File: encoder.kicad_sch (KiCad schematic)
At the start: 0 parts

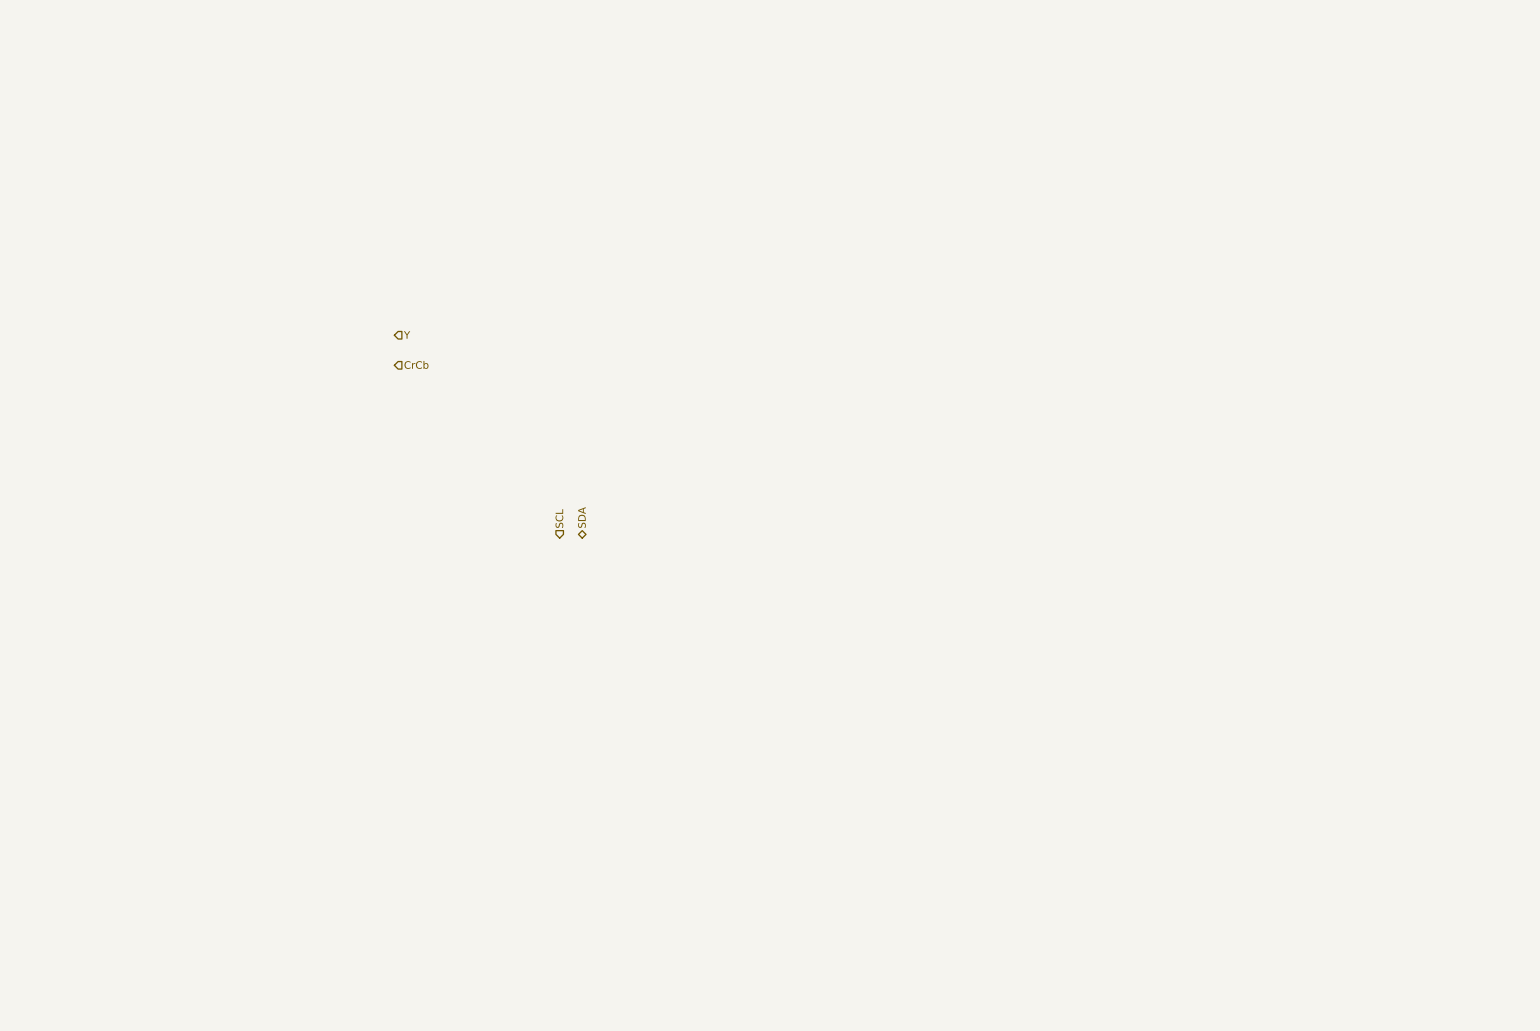
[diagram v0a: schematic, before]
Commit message: added decoder symbol
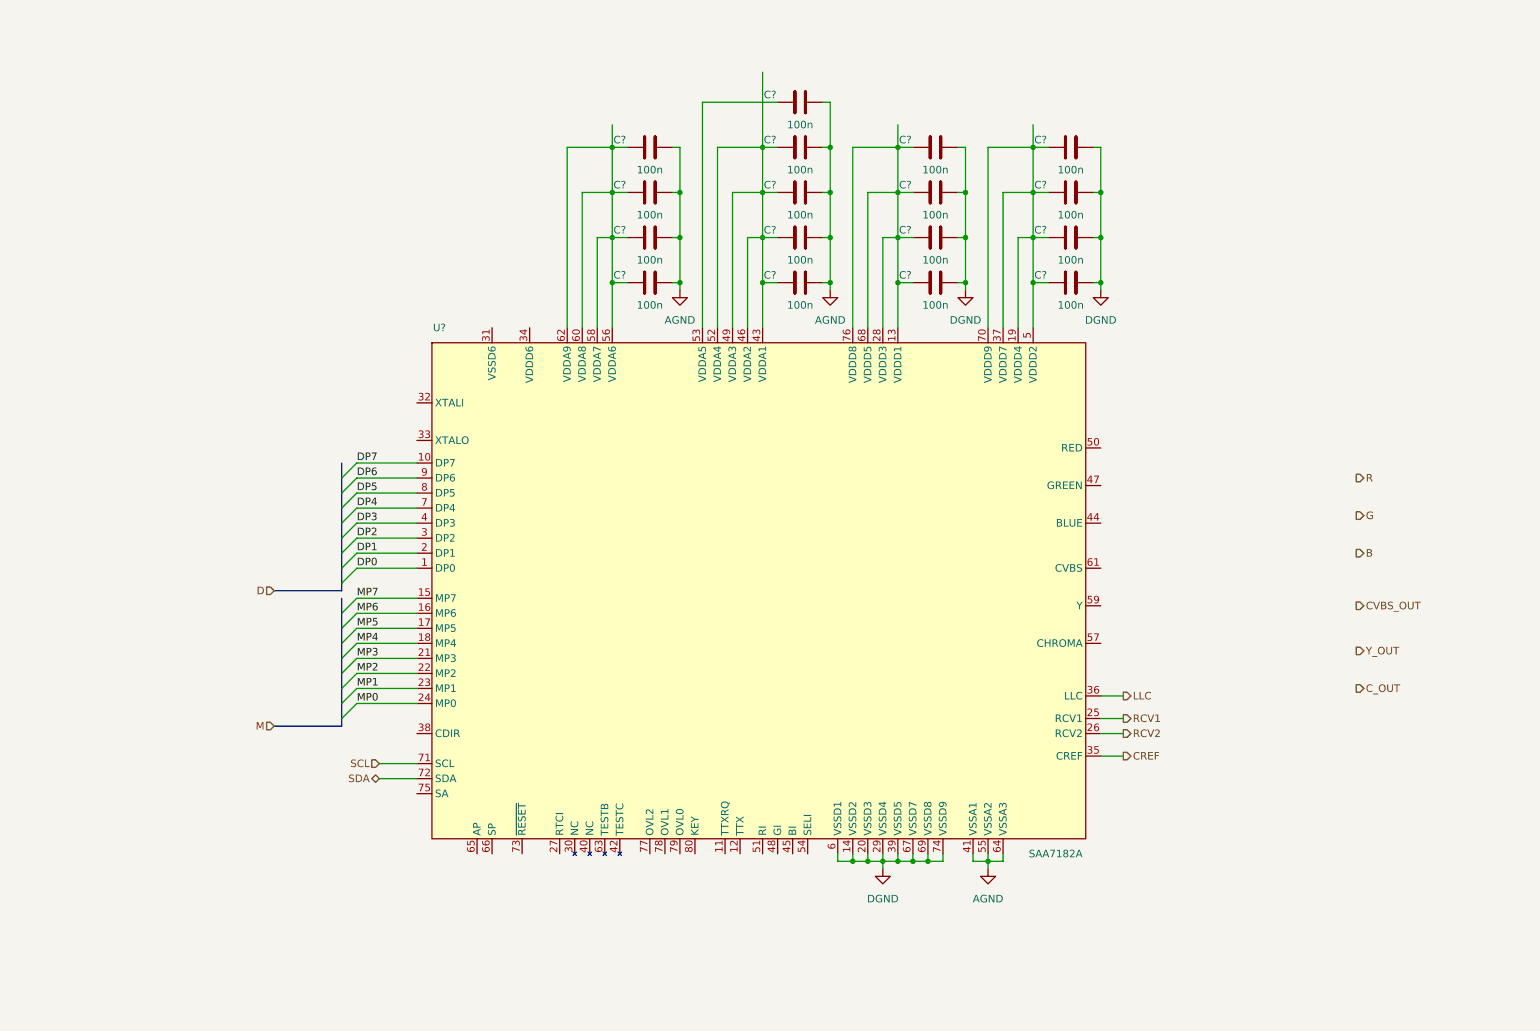
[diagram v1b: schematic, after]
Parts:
- added C? (x17): 100n, symbol tbc:GCJ188R71H104KA12D
- added U?: SAA7182A, symbol tbc:SAA7182A
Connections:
- net SCL: now also U?.71 (SCL)
- net SDA: now also U?.72 (SDA)
- new net: C?.1, C?.1, C?.1, C?.1, U?.13 (VDDD1), U?.28 (VDDD3), U?.68 (VDDD5), U?.76 (VDDD8)
- new net: C?.1, C?.1, C?.1, C?.1, U?.43 (VDDA1), U?.46 (VDDA2), U?.49 (VDDA3), U?.52 (VDDA4)
- new net: C?.1, C?.1, C?.1, C?.1, U?.56 (VDDA6), U?.58 (VDDA7), U?.60 (VDDA8), U?.62 (VDDA9)
- new net: C?.1, C?.1, C?.1, C?.1, U?.19 (VDDD4), U?.37 (VDDD7), U?.5 (VDDD2), U?.70 (VDDD9)
- new net: C?.1, U?.53 (VDDA5)
- new net AGND: C?.2, C?.2, C?.2, C?.2, C?.2, C?.2, C?.2, C?.2, C?.2, U?.41 (VSSA1), U?.55 (VSSA2), U?.64 (VSSA3)
- new net CREF: U?.35 (CREF)
- new net DGND: C?.2, C?.2, C?.2, C?.2, C?.2, C?.2, C?.2, C?.2, U?.14 (VSSD2), U?.20 (VSSD3), U?.29 (VSSD4), U?.39 (VSSD5), U?.6 (VSSD1), U?.67 (VSSD7), U?.69 (VSSD8), U?.74 (VSSD9)
- new net DP0: U?.1 (DP0)
- new net DP1: U?.2 (DP1)
- new net DP2: U?.3 (DP2)
- new net DP3: U?.4 (DP3)
- new net DP4: U?.7 (DP4)
- new net DP5: U?.8 (DP5)
- new net DP6: U?.9 (DP6)
- new net DP7: U?.10 (DP7)
- new net LLC: U?.36 (LLC)
- new net MP0: U?.24 (MP0)
- new net MP1: U?.23 (MP1)
- new net MP2: U?.22 (MP2)
- new net MP3: U?.21 (MP3)
- new net MP4: U?.18 (MP4)
- new net MP5: U?.17 (MP5)
- new net MP6: U?.16 (MP6)
- new net MP7: U?.15 (MP7)
- new net RCV1: U?.25 (RCV1)
- new net RCV2: U?.26 (RCV2)

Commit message: added buses, title block info
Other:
- title: (none) -> Time Base Corrector and Video Scaler
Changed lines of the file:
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@@
 (kicad_sch (version 20230121) (generator eeschema)
   (paper "A4")
+  (title_block
+    (title "Time Base Corrector and Video Scaler")
+    (date "2024-01-15")
+    (rev "1")
+  )
   (junction (at 179.07 157.48) (diameter 0) (color 0 0 0 0)
   )
@@
     (effects (font (size 1.27 1.27)) (justify left bottom))
   )
+  (label "DP[7..0]" (at 71.12 111.76 0) (fields_autoplaced)
+    (effects (font (size 1.27 1.27)) (justify left bottom))
+  )
   (label "MP2" (at 82.55 125.73 0) (fields_autoplaced)
     (effects (font (size 1.27 1.27)) (justify left bottom))
@@
     (effects (font (size 1.27 1.27)) (justify left bottom))
   )
+  (label "MP[7..0]" (at 71.12 134.62 0) (fields_autoplaced)
+    (effects (font (size 1.27 1.27)) (justify left bottom))
+  )

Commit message: added frame memory symbol and updated schematic
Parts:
- C? (x17): MPN GCJ188R71H104KA12D -> (none)
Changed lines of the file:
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@@
-      (effects (font (size 1.27 1.27)) (justify left) hide)
-    )
-    (property "MPN" "GCJ188R71H104KA12D" (at 166.37 44.45 0) (show_name)
       (effects (font (size 1.27 1.27)) (justify left) hide)
     )
@@
     )
     (property "Datasheet" "https://au.mouser.com/datasheet/2/281/1/GCJ188R71H104KA12_02B-3140350.pdf" (at 166.37 64.77 0) (show_name)
-      (effects (font (size 1.27 1.27)) (justify left) hide)
-    )
-    (property "MPN" "GCJ188R71H104KA12D" (at 166.37 59.69 0) (show_name)
       (effects (font (size 1.27 1.27)) (justify left) hide)
     )
@@
       (effects (font (size 1.27 1.27)) (justify left) hide)
     )
-    (property "MPN" "GCJ188R71H104KA12D" (at 143.51 44.45 0) (show_name)
-      (effects (font (size 1.27 1.27)) (justify left) hide)
-    )
     (property "Mouser" " 81-GCJ188R71H104KA2D" (at 143.51 46.99 0) (show_name)
       (effects (font (size 1.27 1.27)) (justify left) hide)
@@
       (effects (font (size 1.27 1.27)) (justify left) hide)
     )
-    (property "MPN" "GCJ188R71H104KA12D" (at 118.11 52.07 0) (show_name)
-      (effects (font (size 1.27 1.27)) (justify left) hide)
-    )
     (property "Mouser" " 81-GCJ188R71H104KA2D" (at 118.11 54.61 0) (show_name)
       (effects (font (size 1.27 1.27)) (justify left) hide)
@@
       (effects (font (size 1.27 1.27)) (justify left) hide)
     )
-    (property "MPN" "GCJ188R71H104KA12D" (at 166.37 67.31 0) (show_name)
-      (effects (font (size 1.27 1.27)) (justify left) hide)
-    )
     (property "Mouser" " 81-GCJ188R71H104KA2D" (at 166.37 69.85 0) (show_name)
       (effects (font (size 1.27 1.27)) (justify left) hide)
@@
     )
     (property "Datasheet" "https://au.mouser.com/datasheet/2/281/1/GCJ188R71H104KA12_02B-3140350.pdf" (at 143.51 64.77 0) (show_name)
-      (effects (font (size 1.27 1.27)) (justify left) hide)
-    )
-    (property "MPN" "GCJ188R71H104KA12D" (at 143.51 59.69 0) (show_name)
       (effects (font (size 1.27 1.27)) (justify left) hide)
     )
@@
       (effects (font (size 1.27 1.27)) (justify left) hide)
     )
-    (property "MPN" "GCJ188R71H104KA12D" (at 118.11 59.69 0) (show_name)
-      (effects (font (size 1.27 1.27)) (justify left) hide)
-    )
     (property "Mouser" " 81-GCJ188R71H104KA2D" (at 118.11 62.23 0) (show_name)
       (effects (font (size 1.27 1.27)) (justify left) hide)
@@
     )
     (property "Datasheet" "https://au.mouser.com/datasheet/2/281/1/GCJ188R71H104KA12_02B-3140350.pdf" (at 166.37 57.15 0) (show_name)
-      (effects (font (size 1.27 1.27)) (justify left) hide)
-    )
-    (property "MPN" "GCJ188R71H104KA12D" (at 166.37 52.07 0) (show_name)
       (effects (font (size 1.27 1.27)) (justify left) hide)
     )
@@
       (effects (font (size 1.27 1.27)) (justify left) hide)
     )
-    (property "MPN" "GCJ188R71H104KA12D" (at 118.11 44.45 0) (show_name)
-      (effects (font (size 1.27 1.27)) (justify left) hide)
-    )
     (property "Mouser" " 81-GCJ188R71H104KA2D" (at 118.11 46.99 0) (show_name)
       (effects (font (size 1.27 1.27)) (justify left) hide)
@@
     )
     (property "Datasheet" "https://au.mouser.com/datasheet/2/281/1/GCJ188R71H104KA12_02B-3140350.pdf" (at 143.51 72.39 0) (show_name)
-      (effects (font (size 1.27 1.27)) (justify left) hide)
-    )
-    (property "MPN" "GCJ188R71H104KA12D" (at 143.51 67.31 0) (show_name)
       (effects (font (size 1.27 1.27)) (justify left) hide)
     )
@@
       (effects (font (size 1.27 1.27)) (justify left) hide)
     )
-    (property "MPN" "GCJ188R71H104KA12D" (at 189.23 44.45 0) (show_name)
-      (effects (font (size 1.27 1.27)) (justify left) hide)
-    )
     (property "Mouser" " 81-GCJ188R71H104KA2D" (at 189.23 46.99 0) (show_name)
       (effects (font (size 1.27 1.27)) (justify left) hide)
@@
       (effects (font (size 1.27 1.27)) (justify left) hide)
     )
-    (property "MPN" "GCJ188R71H104KA12D" (at 189.23 52.07 0) (show_name)
-      (effects (font (size 1.27 1.27)) (justify left) hide)
-    )
     (property "Mouser" " 81-GCJ188R71H104KA2D" (at 189.23 54.61 0) (show_name)
       (effects (font (size 1.27 1.27)) (justify left) hide)
@@
       (effects (font (size 1.27 1.27)) (justify left) hide)
     )
-    (property "MPN" "GCJ188R71H104KA12D" (at 118.11 67.31 0) (show_name)
-      (effects (font (size 1.27 1.27)) (justify left) hide)
-    )
     (property "Mouser" " 81-GCJ188R71H104KA2D" (at 118.11 69.85 0) (show_name)
       (effects (font (size 1.27 1.27)) (justify left) hide)
@@
       (effects (font (size 1.27 1.27)) (justify left) hide)
     )
-    (property "MPN" "GCJ188R71H104KA12D" (at 143.51 36.83 0) (show_name)
-      (effects (font (size 1.27 1.27)) (justify left) hide)
-    )
     (property "Mouser" " 81-GCJ188R71H104KA2D" (at 143.51 39.37 0) (show_name)
       (effects (font (size 1.27 1.27)) (justify left) hide)
@@
       (effects (font (size 1.27 1.27)) (justify left) hide)
     )
-    (property "MPN" "GCJ188R71H104KA12D" (at 189.23 67.31 0) (show_name)
-      (effects (font (size 1.27 1.27)) (justify left) hide)
-    )
     (property "Mouser" " 81-GCJ188R71H104KA2D" (at 189.23 69.85 0) (show_name)
       (effects (font (size 1.27 1.27)) (justify left) hide)
@@
       (effects (font (size 1.27 1.27)) (justify left) hide)
     )
-    (property "MPN" "GCJ188R71H104KA12D" (at 189.23 59.69 0) (show_name)
-      (effects (font (size 1.27 1.27)) (justify left) hide)
-    )
     (property "Mouser" " 81-GCJ188R71H104KA2D" (at 189.23 62.23 0) (show_name)
       (effects (font (size 1.27 1.27)) (justify left) hide)
@@
       (effects (font (size 1.27 1.27)) (justify left) hide)
     )
-    (property "MPN" "GCJ188R71H104KA12D" (at 143.51 52.07 0) (show_name)
-      (effects (font (size 1.27 1.27)) (justify left) hide)
-    )

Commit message: continued on schematic, added power sheet
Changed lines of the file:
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@@
+    (effects (font (size 1.27 1.27)) (justify left))
+  )
+  (hierarchical_label "ENC_RST" (shape input) (at 238.76 143.51 0) (fields_autoplaced)
     (effects (font (size 1.27 1.27)) (justify left))
   )

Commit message: updates to power, ferrites etc
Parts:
- added C?: 22u|25V, symbol tbc:GRM32ER71E226KE15L
- added L?: 10uH, symbol tbc:DFE201610E-100M=P2
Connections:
- net DGND is gone; now on net GND: C?.2, C?.2, C?.2, C?.2, C?.2, C?.2, C?.2, C?.2, U?.14 (VSSD2), U?.20 (VSSD3), U?.29 (VSSD4), U?.39 (VSSD5), U?.6 (VSSD1), U?.67 (VSSD7), U?.69 (VSSD8), U?.74 (VSSD9)
- net +3V3: now reaches C?.1, C?.1, C?.1, C?.1, U?.13 (VDDD1), U?.28 (VDDD3), U?.68 (VDDD5), U?.76 (VDDD8)
- net +3V3: now also C?.1, C?.1, C?.1, C?.1, C?.1, C?.1, C?.1, C?.1, U?.19 (VDDD4), U?.37 (VDDD7), U?.43 (VDDA1), U?.46 (VDDA2), U?.49 (VDDA3), U?.5 (VDDD2), U?.52 (VDDA4), U?.70 (VDDD9), L?.1
- net at C?.1, C?.1, C?.1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: now also C?.1, L?.2
- net AGND renamed GND
- net GND: now also C?.2

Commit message: major progress with memory interfacing
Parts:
- added C? (x2): 100n, symbol tbc:GCJ188R71H104KA12D
- added R?: 2K2, symbol tbc:RC0603FR-072K2L
- added U?: SN74LS74ADR, symbol tbc:SN74LS74ADR
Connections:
- net +3V3: now also C?.1, R?.1, U?.14 (VCC)
- net ENC_RST: now also U?.73 (~{RESET}), C?.2, R?.2
- net GND: now also C?.1, C?.2, U?.7 (GND)
- net RCV1: now also U?.2 (1D)
- net RCV2: now also U?.3 (1CLK)
- new net Q1: U?.5 (1Q)
- new net Q2: U?.6 (1~{Q})
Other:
- moved on the sheet: C?, L?, U?

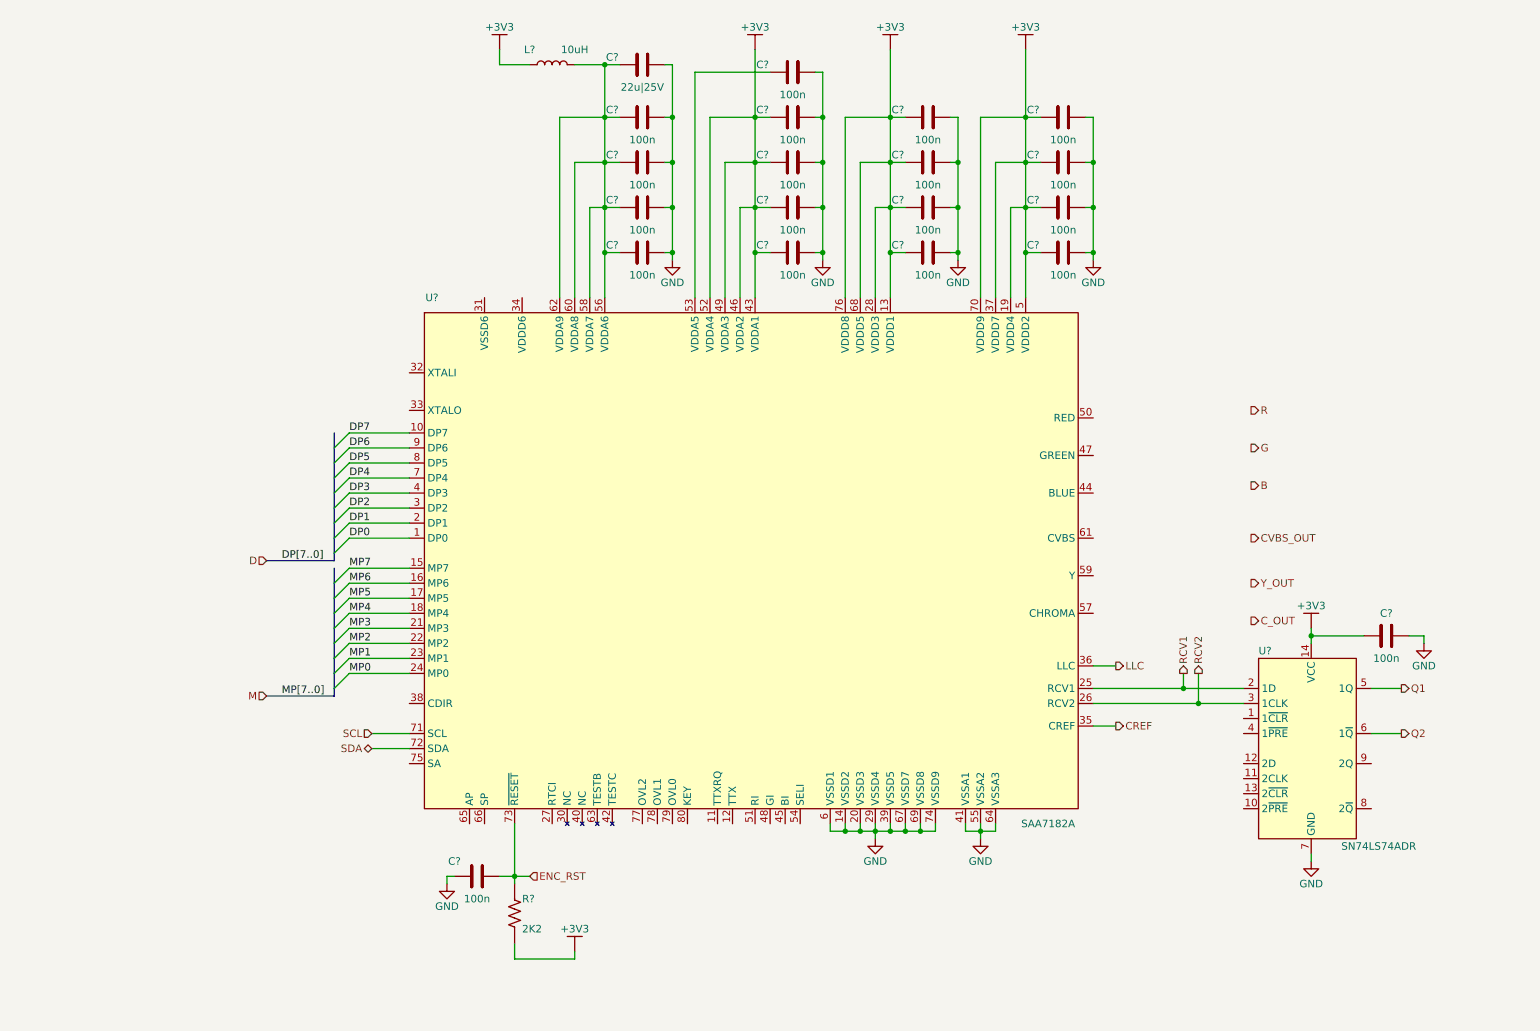
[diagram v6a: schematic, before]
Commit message: minor changes to schematic layout
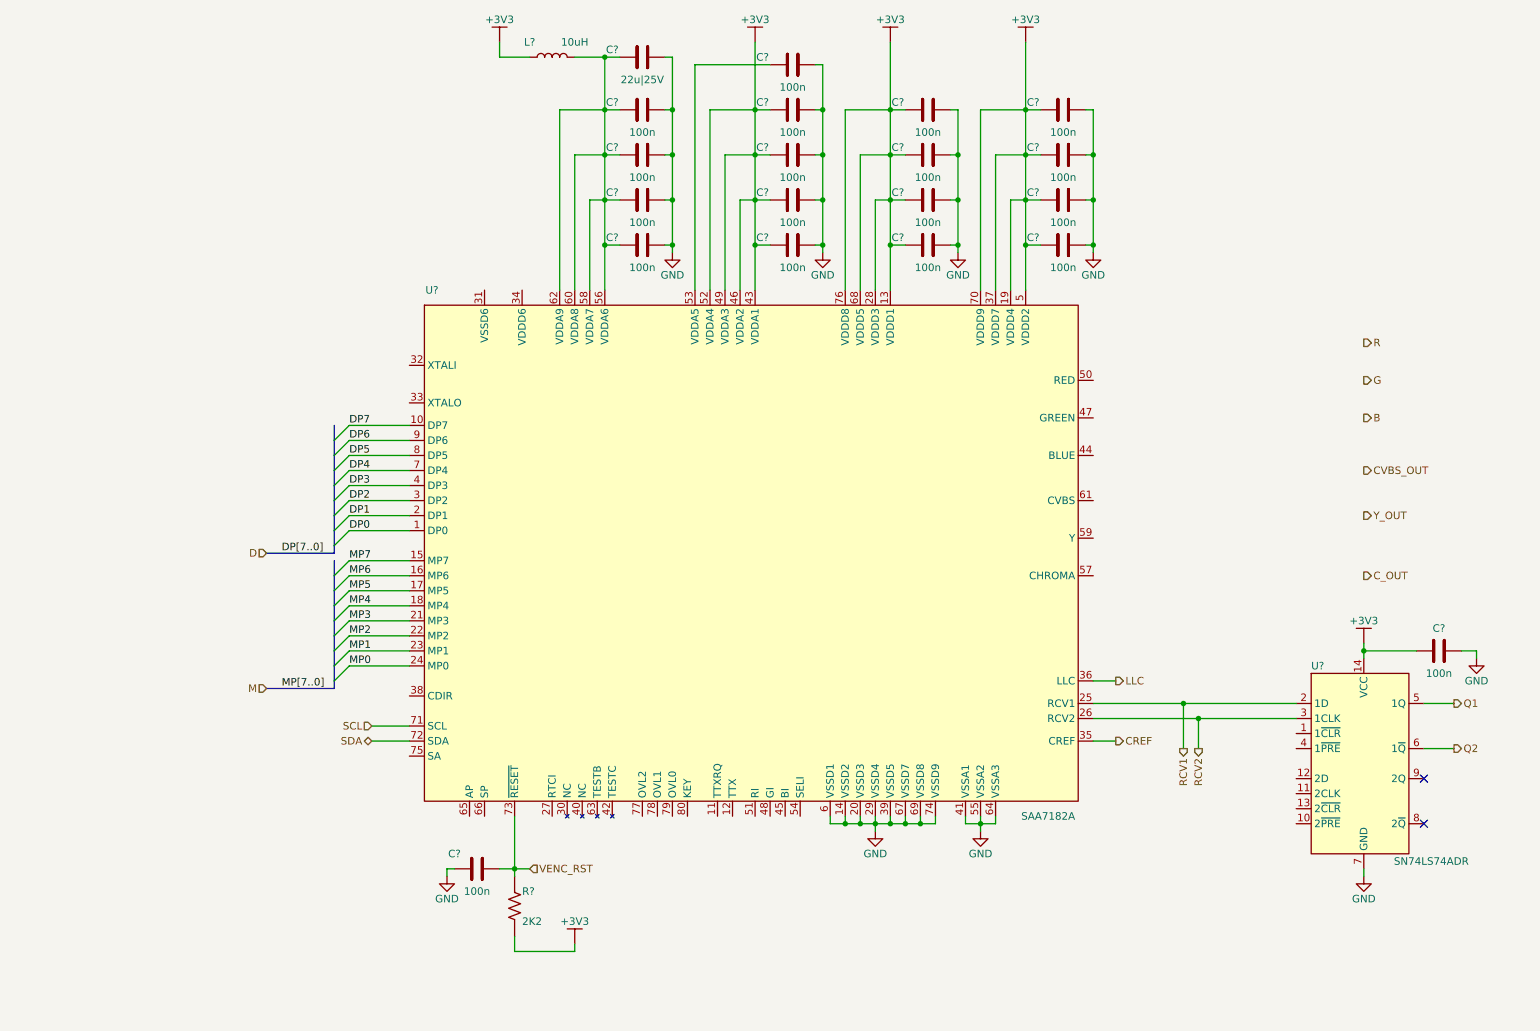
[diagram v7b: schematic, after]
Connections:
- net ENC_RST renamed VENC_RST
- no-connect marks 0 -> 2
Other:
- moved on the sheet: C?, L?, R?, U?
